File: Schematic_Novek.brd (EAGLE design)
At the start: 160 x 100 mm, 30 parts, among them IC1 STM32F10XCXT6, U1 BQ21040, U2 MAX17048G+T10

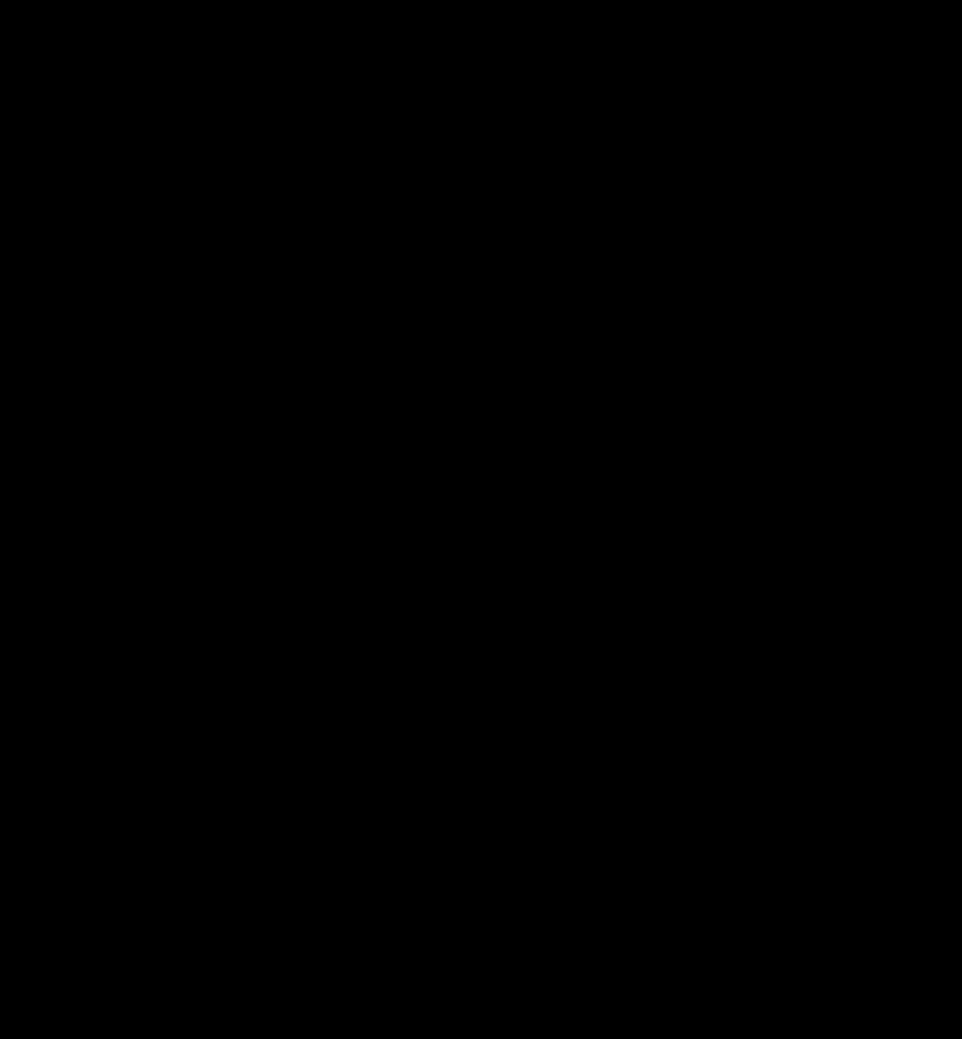
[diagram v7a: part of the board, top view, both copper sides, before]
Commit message: Adds pressure gauge
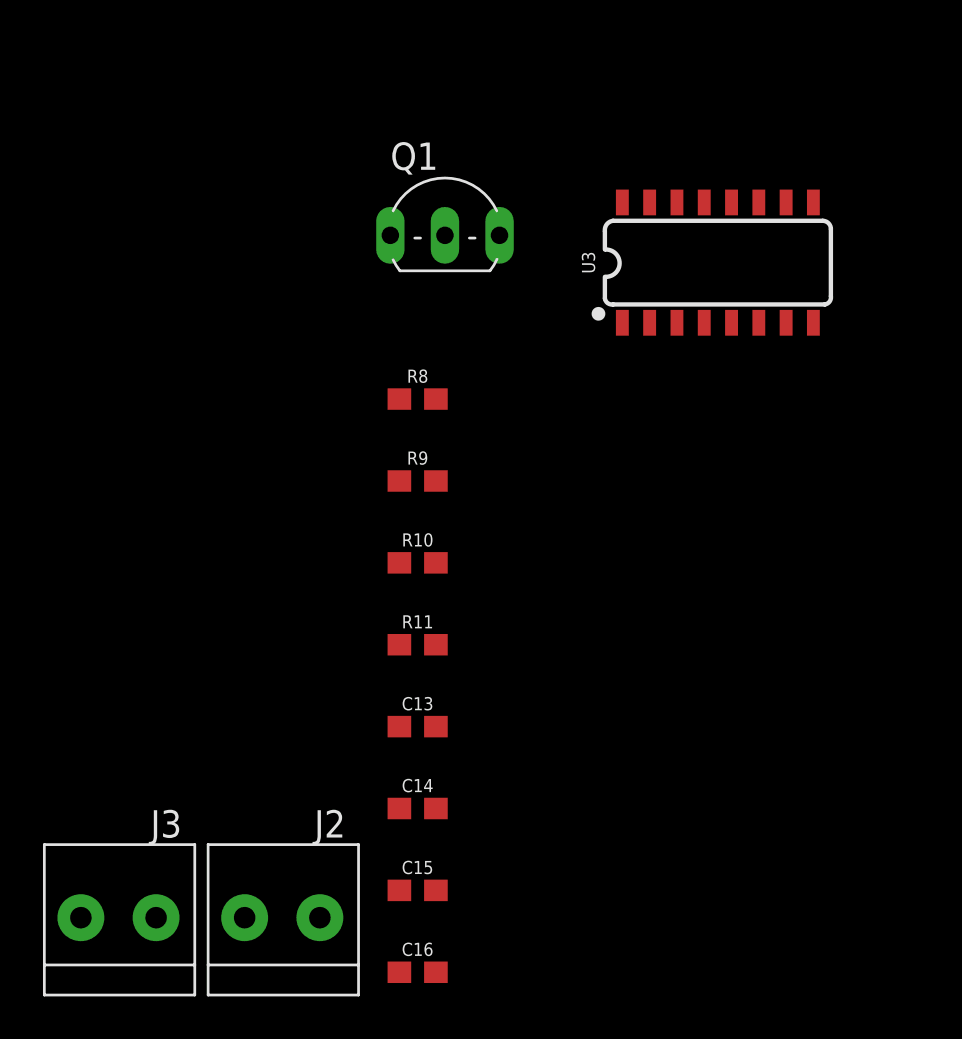
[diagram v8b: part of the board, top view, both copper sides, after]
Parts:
- added C13, C14: 0.1uF, SparkFun-Capacitors:0603
- added C15, C16: 10uF, SparkFun-Capacitors:0603
- added J2, J3: 1X2-3.5MM, adafruit:1X2-3.5MM
- added Q1: 2N2907, adafruit:TO92-EBC-OVAL
- added R10, R11: 100, SparkFun-Resistors:0603
- added R8: 20k, SparkFun-Resistors:0603
- added R9: 8.2k, SparkFun-Resistors:0603
- added U3: HX711, SparkFun-IC-Conversion:SO16
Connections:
- new net DOUT_HX: U3.12
- new net N$10: C13.2, U3.6
- new net N$11: R8.2, R9.1, U3.4
- new net N$12: C14.1, R10.1, U3.7
- new net N$13: C14.2, R11.1, U3.8
- new net N$5: Q1.B, U3.2
- new net N$6: C15.2, Q1.E, U3.1, U3.16
- new net N$7: C16.1, J2.2, Q1.C, R8.1, U3.3
- new net N$8: J3.2, R10.2
- new net N$9: J3.1, R11.2
- new net SCK_HX: U3.11
- net GND: now also C13.1, C15.1, C16.2, R9.2, U3.10, U3.14, U3.15, U3.5, U3.9
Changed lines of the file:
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@@
 <attribute name="VALUE" x="-26.67" y="-145.542" size="0.6096" layer="27" font="vector" ratio="20" align="top-center"/>
+</element>
+<element name="U3" library="SparkFun-IC-Conversion" package="SO16" value="HX711" x="-21.59" y="-177.8" smashed="yes">
+<attribute name="NAME" x="-27.305" y="-177.8" size="0.6096" layer="25" font="vector" ratio="20" rot="R90" align="bottom-center"/>
+<attribute name="PROD_ID" value="IC-12445" x="-21.59" y="-177.8" size="1.778" layer="27" display="off"/>
+<attribute name="VALUE" x="-15.24" y="-177.8" size="0.6096" layer="27" font="vector" ratio="20" rot="R90" align="bottom-center"/>
+</element>
+<element name="Q1" library="adafruit" package="TO92-EBC-OVAL" value="2N2907" x="-34.29" y="-175.26" smashed="yes">
+<attribute name="NAME" x="-36.83" y="-173.482" size="1.27" layer="25" ratio="10"/>
+<attribute name="VALUE" x="-36.83" y="-179.832" size="1.27" layer="27" ratio="10"/>
+</element>
+<element name="R8" library="SparkFun-Resistors" package="0603" value="20k" x="-35.56" y="-184.15" smashed="yes">
+<attribute name="NAME" x="-35.56" y="-183.388" size="0.6096" layer="25" font="vector" ratio="20" align="bottom-center"/>
+<attribute name="PROD_ID" value="RES-09383" x="-35.56" y="-184.15" size="1.778" layer="27" display="off"/>
+<attribute name="VALUE" x="-35.56" y="-184.912" size="0.6096" layer="27" font="vector" ratio="20" align="top-center"/>
+</element>
+<element name="R9" library="SparkFun-Resistors" package="0603" value="8.2k" x="-35.56" y="-187.96" smashed="yes">
+<attribute name="NAME" x="-35.56" y="-187.198" size="0.6096" layer="25" font="vector" ratio="20" align="bottom-center"/>
+<attribute name="PROD_ID" value="RES-10646" x="-35.56" y="-187.96" size="1.778" layer="27" display="off"/>
+<attribute name="VALUE" x="-35.56" y="-188.722" size="0.6096" layer="27" font="vector" ratio="20" align="top-center"/>
+</element>
+<element name="R10" library="SparkFun-Resistors" package="0603" value="100" x="-35.56" y="-191.77" smashed="yes">
+<attribute name="NAME" x="-35.56" y="-191.008" size="0.6096" layer="25" font="vector" ratio="20" align="bottom-center"/>
+<attribute name="PROD_ID" value="RES-07863" x="-35.56" y="-191.77" size="1.778" layer="27" display="off"/>
+<attribute name="VALUE" x="-35.56" y="-192.532" size="0.6096" layer="27" font="vector" ratio="20" align="top-center"/>
+</element>
+<element name="R11" library="SparkFun-Resistors" package="0603" value="100" x="-35.56" y="-195.58" smashed="yes">
+<attribute name="NAME" x="-35.56" y="-194.818" size="0.6096" layer="25" font="vector" ratio="20" align="bottom-center"/>
+<attribute name="PROD_ID" value="RES-07863" x="-35.56" y="-195.58" size="1.778" layer="27" display="off"/>
+<attribute name="VALUE" x="-35.56" y="-196.342" size="0.6096" layer="27" font="vector" ratio="20" align="top-center"/>
+</element>
+<element name="C13" library="SparkFun-Capacitors" package="0603" value="0.1uF" x="-35.56" y="-199.39" smashed="yes">
+<attribute name="NAME" x="-35.56" y="-198.628" size="0.6096" layer="25" font="vector" ratio="20" align="bottom-center"/>
+<attribute name="PROD_ID" value="CAP-08604" x="-35.56" y="-199.39" size="1.778" layer="27" display="off"/>
+<attribute name="VALUE" x="-35.56" y="-200.152" size="0.6096" layer="27" font="vector" ratio="20" align="top-center"/>
+</element>
+<element name="C14" library="SparkFun-Capacitors" package="0603" value="0.1uF" x="-35.56" y="-203.2" smashed="yes">
+<attribute name="NAME" x="-35.56" y="-202.438" size="0.6096" layer="25" font="vector" ratio="20" align="bottom-center"/>
+<attribute name="PROD_ID" value="CAP-08604" x="-35.56" y="-203.2" size="1.778" layer="27" display="off"/>
+<attribute name="VALUE" x="-35.56" y="-203.962" size="0.6096" layer="27" font="vector" ratio="20" align="top-center"/>
+</element>
+<element name="C15" library="SparkFun-Capacitors" package="0603" value="10uF" x="-35.56" y="-207.01" smashed="yes">
+<attribute name="NAME" x="-35.56" y="-206.248" size="0.6096" layer="25" font="vector" ratio="20" align="bottom-center"/>
+<attribute name="PROD_ID" value="CAP-11015" x="-35.56" y="-207.01" size="1.778" layer="27" display="off"/>
+<attribute name="VALUE" x="-35.56" y="-207.772" size="0.6096" layer="27" font="vector" ratio="20" align="top-center"/>
+</element>
+<element name="C16" library="SparkFun-Capacitors" package="0603" value="10uF" x="-35.56" y="-210.82" smashed="yes">
+<attribute name="NAME" x="-35.56" y="-210.058" size="0.6096" layer="25" font="vector" ratio="20" align="bottom-center"/>
+<attribute name="PROD_ID" value="CAP-11015" x="-35.56" y="-210.82" size="1.778" layer="27" display="off"/>
+<attribute name="VALUE" x="-35.56" y="-211.582" size="0.6096" layer="27" font="vector" ratio="20" align="top-center"/>
+</element>
+<element name="J2" library="adafruit" package="1X2-3.5MM" value="1X2-3.5MM" x="-41.91" y="-208.28" smashed="yes">
+<attribute name="NAME" x="-38.91" y="-203.28" size="1.27" layer="25" rot="R180"/>
+</element>
+<element name="J3" library="adafruit" package="1X2-3.5MM" value="1X2-3.5MM" x="-49.53" y="-208.28" smashed="yes">
+<attribute name="NAME" x="-46.53" y="-203.28" size="1.27" layer="25" rot="R180"/>
 </element>
 </elements>
@@
 <contactref element="U2" pad="1"/>
 <contactref element="U2" pad="6"/>
+<contactref element="C15" pad="1"/>
+<contactref element="C13" pad="1"/>
+<contactref element="C16" pad="2"/>
+<contactref element="R9" pad="2"/>
+<contactref element="U3" pad="5"/>
+<contactref element="U3" pad="15"/>
+<contactref element="U3" pad="14"/>
+<contactref element="U3" pad="10"/>
+<contactref element="U3" pad="9"/>
+<wire x1="-36.41" y1="-207.01" x2="-34.71" y2="-210.82" width="0" layer="19" extent="1-1"/>
+<wire x1="-36.41" y1="-199.39" x2="-36.41" y2="-207.01" width="0" layer="19" extent="1-1"/>
+<wire x1="-34.71" y1="-187.96" x2="-36.41" y2="-199.39" width="0" layer="19" extent="1-1"/>
+<wire x1="-20.955" y1="-180.6" x2="-34.71" y2="-187.96" width="0" layer="19" extent="1-1"/>
+<wire x1="-23.495" y1="-175" x2="-20.955" y2="-180.6" width="0" layer="19" extent="1-1"/>
+<wire x1="-24.765" y1="-175" x2="-23.495" y2="-175" width="0" layer="19" extent="1-1"/>
+<wire x1="-18.415" y1="-175" x2="-23.495" y2="-175" width="0" layer="19" extent="1-1"/>
+<wire x1="-17.145" y1="-175" x2="-18.415" y2="-175" width="0" layer="19" extent="1-1"/>
+<wire x1="-25.82" y1="-144.78" x2="-24.765" y2="-175" width="0" layer="19" extent="1-1"/>
 <wire x1="-26.385" y1="-134.1" x2="-25.82" y2="-144.78" width="0" layer="19" extent="1-1"/>
 <wire x1="-26.385" y1="-132.6" x2="-26.385" y2="-134.1" width="0" layer="19" extent="1-1"/>
@@
 <contactref element="U2" pad="9"/>
 </signal>
+<signal name="N$6">
+<contactref element="U3" pad="16"/>
+<contactref element="C15" pad="2"/>
+<contactref element="U3" pad="1"/>
+<contactref element="Q1" pad="E"/>
+<wire x1="-26.035" y1="-180.6" x2="-34.71" y2="-207.01" width="0" layer="19" extent="1-1"/>
+<wire x1="-26.035" y1="-175" x2="-26.035" y2="-180.6" width="0" layer="19" extent="1-1"/>
+<wire x1="-36.83" y1="-176.53" x2="-26.035" y2="-175" width="0" layer="19" extent="1-1"/>
+</signal>
+<signal name="N$5">
+<contactref element="U3" pad="2"/>
+<contactref element="Q1" pad="B"/>
+<wire x1="-24.765" y1="-180.6" x2="-34.29" y2="-176.53" width="0" layer="19" extent="1-1"/>
+</signal>
+<signal name="N$7">
+<contactref element="U3" pad="3"/>
+<contactref element="J2" pad="2"/>
+<contactref element="C16" pad="1"/>
+<contactref element="R8" pad="1"/>
+<contactref element="Q1" pad="C"/>
+<wire x1="-36.41" y1="-210.82" x2="-43.61" y2="-208.28" width="0" layer="19" extent="1-1"/>
+<wire x1="-36.41" y1="-184.15" x2="-43.61" y2="-208.28" width="0" layer="19" extent="1-1"/>
+<wire x1="-31.75" y1="-176.53" x2="-36.41" y2="-184.15" width="0" layer="19" extent="1-1"/>
+<wire x1="-23.495" y1="-180.6" x2="-31.75" y2="-176.53" width="0" layer="19" extent="1-1"/>
+</signal>
+<signal name="N$11">
+<contactref element="R8" pad="2"/>
+<contactref element="R9" pad="1"/>
+<contactref element="U3" pad="4"/>
+<wire x1="-34.71" y1="-184.15" x2="-36.41" y2="-187.96" width="0" layer="19" extent="1-1"/>
+<wire x1="-22.225" y1="-180.6" x2="-34.71" y2="-184.15" width="0" layer="19" extent="1-1"/>
+</signal>
+<signal name="N$10">
+<contactref element="U3" pad="6"/>
+<contactref element="C13" pad="2"/>
+<wire x1="-19.685" y1="-180.6" x2="-34.71" y2="-199.39" width="0" layer="19" extent="1-1"/>
+</signal>
+<signal name="N$12">
+<contactref element="U3" pad="7"/>
+<contactref element="R10" pad="1"/>
+<contactref element="C14" pad="1"/>
+<wire x1="-36.41" y1="-191.77" x2="-36.41" y2="-203.2" width="0" layer="19" extent="1-1"/>
+<wire x1="-18.415" y1="-180.6" x2="-36.41" y2="-191.77" width="0" layer="19" extent="1-1"/>
+</signal>
+<signal name="N$13">
+<contactref element="U3" pad="8"/>
+<contactref element="R11" pad="1"/>
+<contactref element="C14" pad="2"/>
+<wire x1="-36.41" y1="-195.58" x2="-34.71" y2="-203.2" width="0" layer="19" extent="1-1"/>
+<wire x1="-17.145" y1="-180.6" x2="-36.41" y2="-195.58" width="0" layer="19" extent="1-1"/>
+</signal>
+<signal name="N$8">
+<contactref element="J3" pad="2"/>
+<contactref element="R10" pad="2"/>
+<wire x1="-51.23" y1="-208.28" x2="-34.71" y2="-191.77" width="0" layer="19" extent="1-1"/>
+</signal>
+<signal name="N$9">
+<contactref element="R11" pad="2"/>
+<contactref element="J3" pad="1"/>
+<wire x1="-47.73" y1="-208.28" x2="-34.71" y2="-195.58" width="0" layer="19" extent="1-1"/>
+</signal>
+<signal name="DOUT_HX">
+<contactref element="U3" pad="12"/>
+</signal>
+<signal name="SCK_HX">
+<contactref element="U3" pad="11"/>
+</signal>
 </signals>
